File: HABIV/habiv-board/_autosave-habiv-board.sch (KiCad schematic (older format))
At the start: 122 parts, among them IC1 RTC_PCF8523T, J1 Micro_SD_Card_Det, J10 Conn_01x02_Female, J11 Conn_01x02_Female, J12 Conn_01x02_Female, J13 Conn_01x02_Female, J14 Conn_01x02_Female, J15 Conn_01x02_Female, J16 Conn_01x02_Female, J18 Conn_01x03_Male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

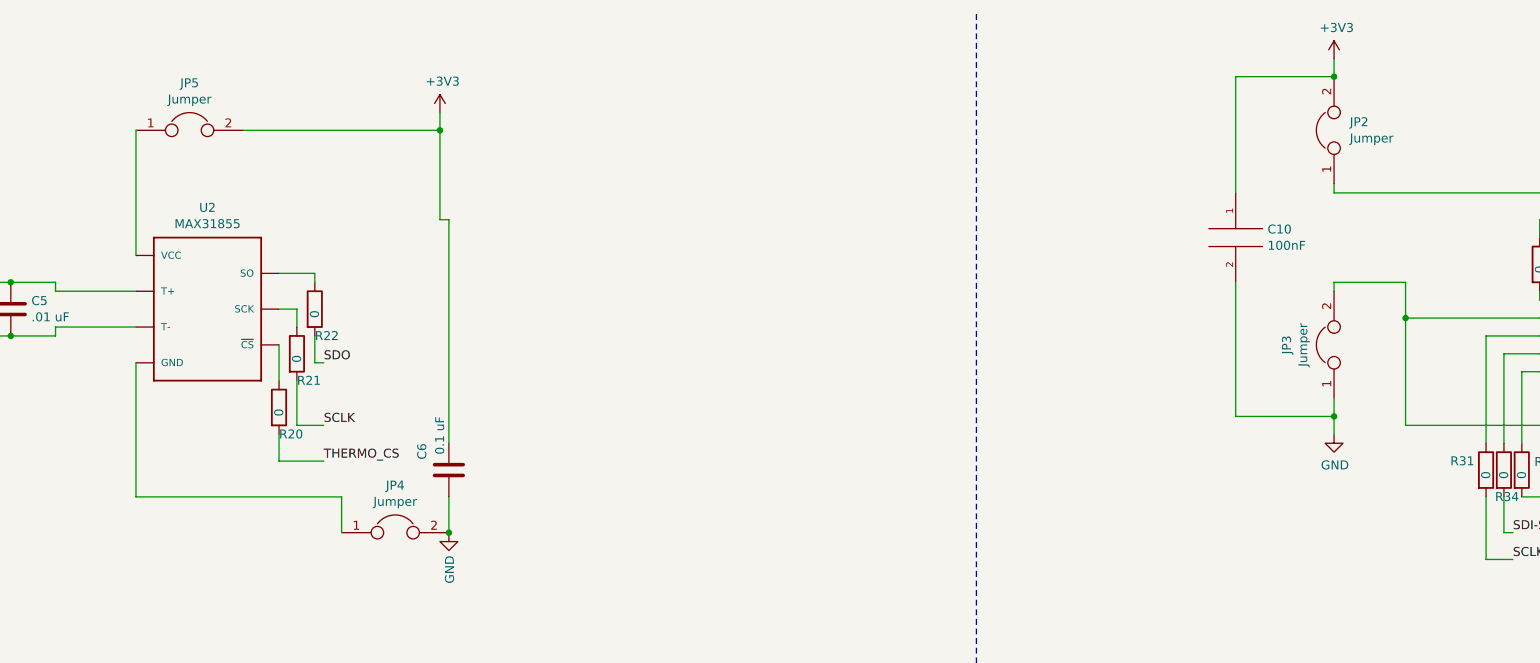
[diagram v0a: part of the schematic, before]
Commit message: first commit adding HABV
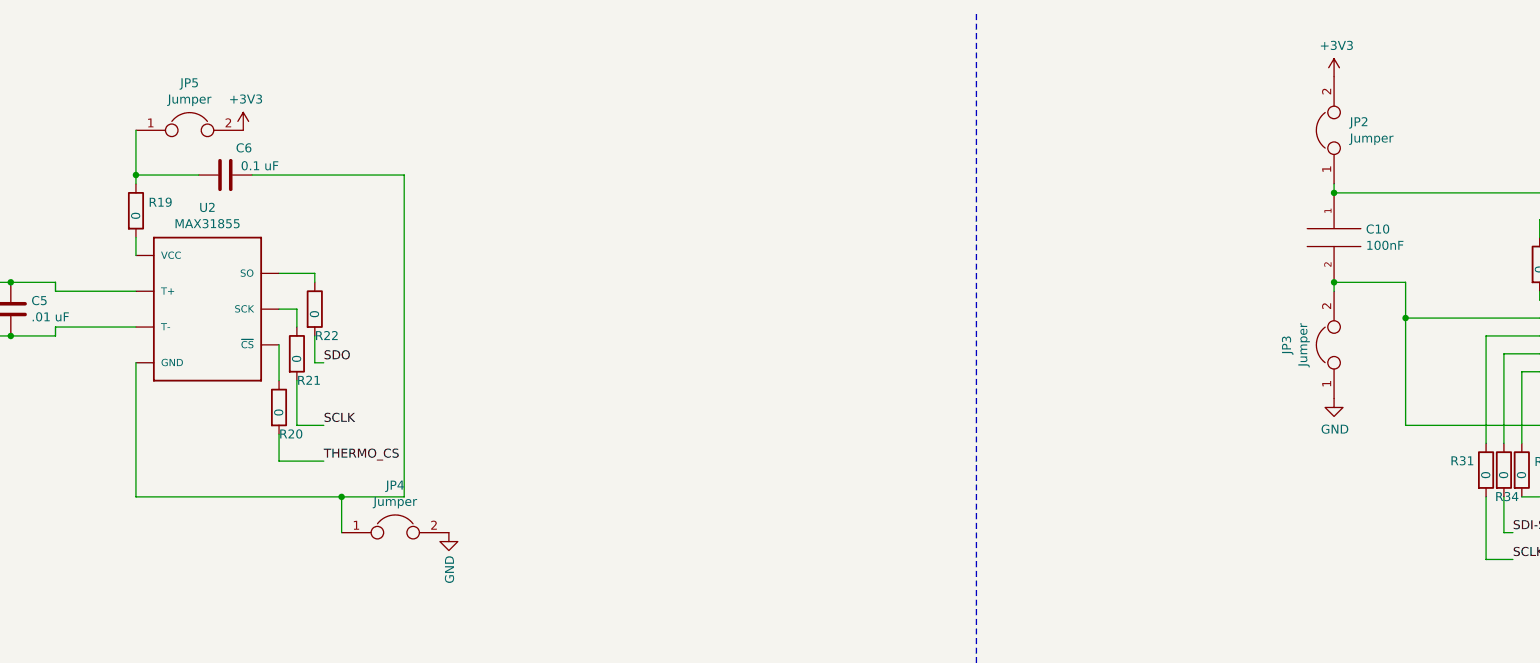
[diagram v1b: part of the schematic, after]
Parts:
- added R19: 0, Resistor_SMD:R_0805_2012Metric, symbol Device:R
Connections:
- net +3V3: no longer C10.1, C6.2
- net GND: no longer C10.2, C6.1
- net at JP2.1, U7.1 (VDD): now also C10.1
- net at JP3.2, U7.2 (PS), U7.3 (GND): now also C10.2
- net at JP4.1, U2.1 (GND): now also C6.2
- net at U2.4 (VCC): now also R19.2; no longer JP5.1
- new net: C6.1, JP5.1, R19.1
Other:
- moved on the sheet: C10, C6
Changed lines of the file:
@@
 L Device:C C6
 U 1 1 5BB5DB50
-P 11250 3050
-F 0 "C6" V 11400 2900 50  0000 L CNN
-F 1 "0.1 uF" V 11300 2750 50  0000 L CNN
-F 2 "Capacitor_SMD:C_0805_2012Metric" H 11288 2900 50  0001 C CNN
-F 3 "~" H 11250 3050 50  0001 C CNN
-	1    11250 3050
-	-1   0    0    1
+P 10000 1400
+F 0 "C6" V 10150 1250 50  0000 L CNN
+F 1 "0.1 uF" V 10050 1100 50  0000 L CNN
+F 2 "Capacitor_SMD:C_0805_2012Metric" H 10038 1250 50  0001 C CNN
+F 3 "~" H 10000 1400 50  0001 C CNN
+	1    10000 1400
+	0    -1   -1   0
 $EndComp
 Wire Wire Line
+	9500 1400 9850 1400
+Wire Wire Line
+	9500 1400 9500 1450
+Wire Wire Line
 	9500 2450 9500 3200
 Wire Wire Line
 	9500 3200 10650 3200
 Wire Wire Line
+	9500 1400 9500 1150
+Connection ~ 9500 1400
+Wire Wire Line
 	10300 2150 10400 2150
 Wire Wire Line
@@
 L pspice:CAP C10
 U 1 1 5BB5E0FC
-P 15650 1750
-F 0 "C10" H 15828 1796 50  0000 L CNN
-F 1 "100nF" H 15828 1705 50  0000 L CNN
-F 2 "Capacitor_SMD:C_0805_2012Metric" H 15650 1750 50  0001 C CNN
-F 3 "" H 15650 1750 50  0001 C CNN
-	1    15650 1750
+P 16200 1750
+F 0 "C10" H 16378 1796 50  0000 L CNN
+F 1 "100nF" H 16378 1705 50  0000 L CNN
+F 2 "Capacitor_SMD:C_0805_2012Metric" H 16200 1750 50  0001 C CNN
+F 3 "" H 16200 1750 50  0001 C CNN
+	1    16200 1750
 	1    0    0    -1
 $EndComp
@@
 L power:+3V3 #PWR028
 U 1 1 5BB5E5DC
-P 16200 750
-F 0 "#PWR028" H 16200 600 50  0001 C CNN
-F 1 "+3V3" H 16215 923 50  0000 C CNN
-F 2 "" H 16200 750 50  0001 C CNN
-F 3 "" H 16200 750 50  0001 C CNN
-	1    16200 750
+P 16200 850
+F 0 "#PWR028" H 16200 700 50  0001 C CNN
+F 1 "+3V3" H 16215 1023 50  0000 C CNN
+F 2 "" H 16200 850 50  0001 C CNN
+F 3 "" H 16200 850 50  0001 C CNN
+	1    16200 850
 	1    0    0    -1
 $EndComp
@@
 L power:GND #PWR029
 U 1 1 5BB5E65F
-P 16200 2850
-F 0 "#PWR029" H 16200 2600 50  0001 C CNN
-F 1 "GND" H 16205 2677 50  0000 C CNN
-F 2 "" H 16200 2850 50  0001 C CNN
-F 3 "" H 16200 2850 50  0001 C CNN
-	1    16200 2850
+P 16200 2650
+F 0 "#PWR029" H 16200 2400 50  0001 C CNN
+F 1 "GND" H 16205 2477 50  0000 C CNN
+F 2 "" H 16200 2650 50  0001 C CNN
+F 3 "" H 16200 2650 50  0001 C CNN
+	1    16200 2650
 	1    0    0    -1
 $EndComp
@@
 Wire Wire Line
 	16200 1450 16200 1500
+Connection ~ 16200 1500
 $Comp
 L habiv-board-rescue:STM32F401RET6-STM32-rescue U1
@@
 Wire Wire Line
 	5650 13850 5650 13950
+$Comp
+L Device:R R19
+U 1 1 5D15D3CF
+P 9500 1600
+F 0 "R19" H 9570 1646 50  0000 L CNN
+F 1 "0" V 9500 1550 50  0000 L CNN
+F 2 "Resistor_SMD:R_0805_2012Metric" V 9430 1600 50  0001 C CNN
+F 3 "~" H 9500 1600 50  0001 C CNN
+	1    9500 1600
+	1    0    0    -1
+$EndComp
+Wire Wire Line
+	9500 1750 9500 1850
 Wire Wire Line
 	5000 6800 5000 7350
@@
 Wire Wire Line
 	10650 3400 10650 3200
+Wire Wire Line
+	11000 1400 11000 3200
+Wire Wire Line
+	11000 3200 10650 3200
+Wire Wire Line
+	10150 1400 11000 1400
+Connection ~ 10650 3200
 $Comp
 L power:+3V3 #PWR026
 U 1 1 5D5B869B
-P 11200 1050
-F 0 "#PWR026" H 11200 900 50  0001 C CNN
-F 1 "+3V3" H 11215 1223 50  0000 C CNN
-F 2 "" H 11200 1050 50  0001 C CNN
-F 3 "" H 11200 1050 50  0001 C CNN
-	1    11200 1050
+P 10100 1150
+F 0 "#PWR026" H 10100 1000 50  0001 C CNN
+F 1 "+3V3" H 10115 1323 50  0000 C CNN
+F 2 "" H 10100 1150 50  0001 C CNN
+F 3 "" H 10100 1150 50  0001 C CNN
+	1    10100 1150
 	1    0    0    -1
 $EndComp
@@
 Wire Wire Line
 	16200 2050 16200 2000
+Connection ~ 16200 2000
 $Comp
 L power:+5V #PWR0101
@@
 	2850 2050 2850 2150
 Connection ~ 2850 2150
-Wire Wire Line
-	11250 3200 11250 3400
-Connection ~ 11250 3400
-Wire Wire Line
-	9500 1150 9500 1850
-Wire Wire Line
-	11250 2900 11250 1650
-Wire Wire Line
-	11250 1650 11200 1650
-Wire Wire Line
-	11200 1650 11200 1150
-Wire Wire Line
-	10100 1150 11200 1150
-Connection ~ 11200 1150
-Wire Wire Line
-	11200 1150 11200 1050
-Wire Wire Line
-	16200 750  16200 850
-Wire Wire Line
-	16200 2850 16200 2750
-Wire Wire Line
-	15650 2000 15650 2750
-Wire Wire Line
-	15650 2750 16200 2750
-Connection ~ 16200 2750
-Wire Wire Line
-	16200 2750 16200 2650
-Wire Wire Line
-	16200 850  15650 850
-Wire Wire Line
-	15650 850  15650 1500
-Connection ~ 16200 850
 $EndSCHEMATC
